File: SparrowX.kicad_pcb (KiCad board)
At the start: 4 copper layers, 31.6 x 26.6 mm, 31 parts, among them J1 NORTH, J2 SOUTH, J3 WEST, J4 EAST, U1 LMR43610MSC3RPERQ1, U2 LD49100PU33RY, U3 STM32G0B1CBU6, U4 TCAN332G, U5 TCAN332G

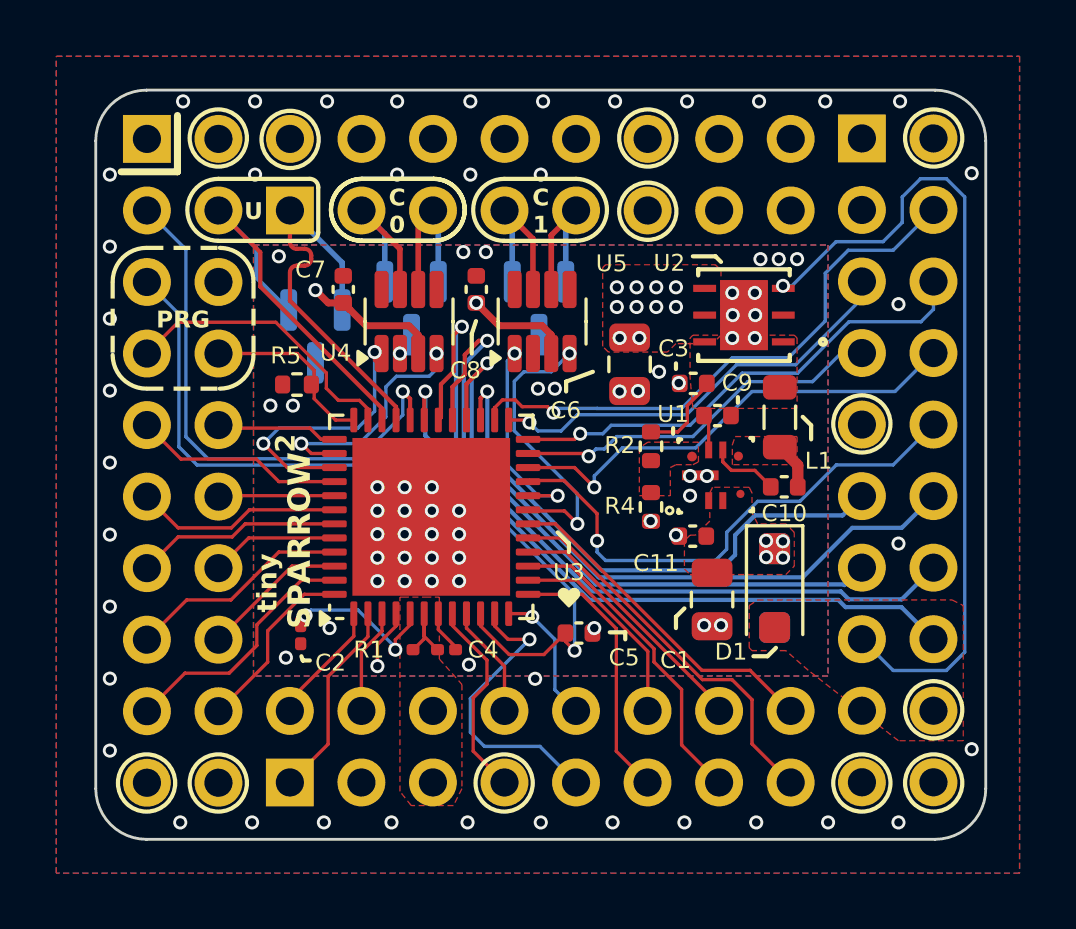
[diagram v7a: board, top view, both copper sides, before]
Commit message: More silkscreen tweaks
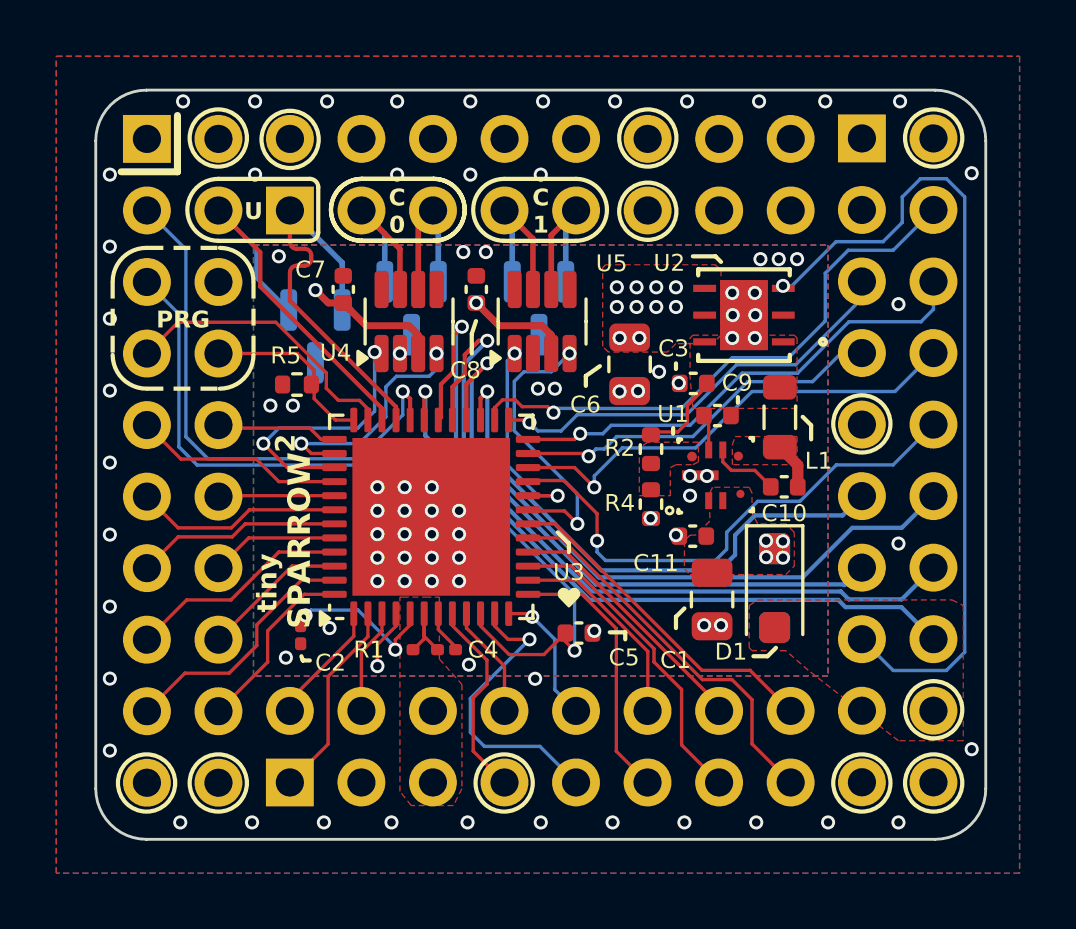
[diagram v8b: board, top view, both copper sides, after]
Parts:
- moved R2 0.10 mm to (174.3, 93.5)
- moved R4 0.10 mm to (174.3, 95.5)
